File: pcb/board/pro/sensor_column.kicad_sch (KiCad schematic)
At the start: 3 parts, among them U210 CD74HC4067SM96

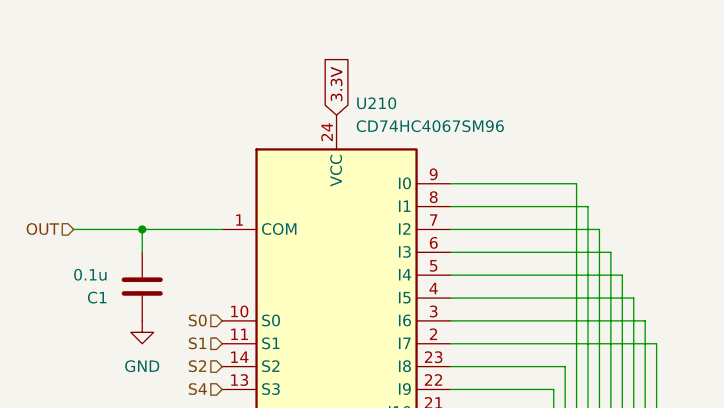
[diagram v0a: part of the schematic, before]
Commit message: Updated with filter caps
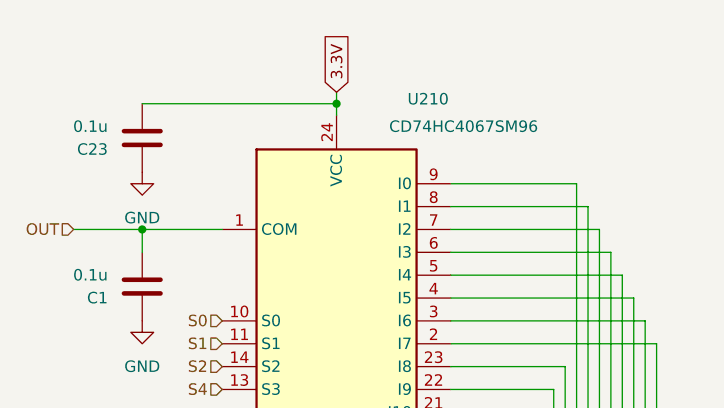
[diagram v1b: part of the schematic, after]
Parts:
- added C23: 0.1u, Capacitor_SMD:C_0402_1005Metric, symbol Device:C
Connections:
- net 3.3V: now also C23.2
- net GND: now also C23.1
